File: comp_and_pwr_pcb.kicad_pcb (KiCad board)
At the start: 2 copper layers, 2 parts, among them J2 Conn_01x02, U1 RP2040

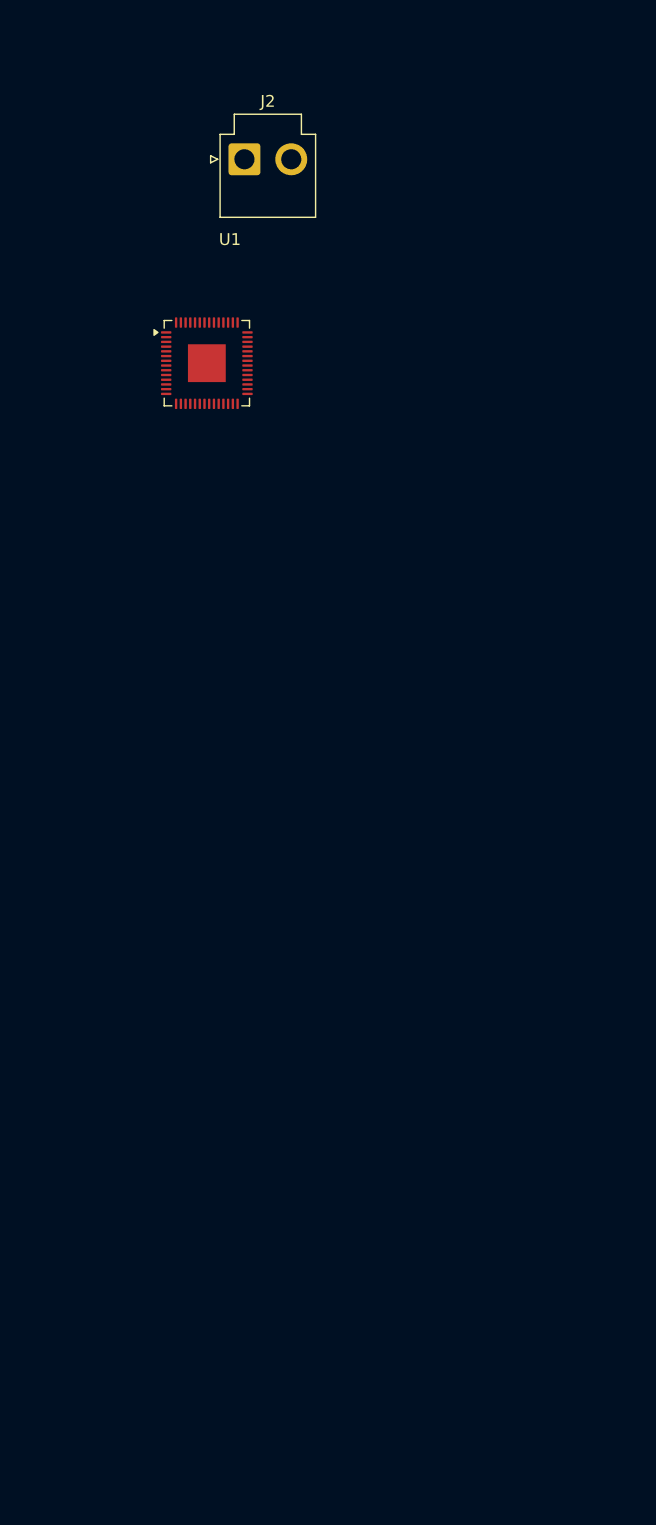
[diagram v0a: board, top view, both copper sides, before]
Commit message: Footprints added and layout finished
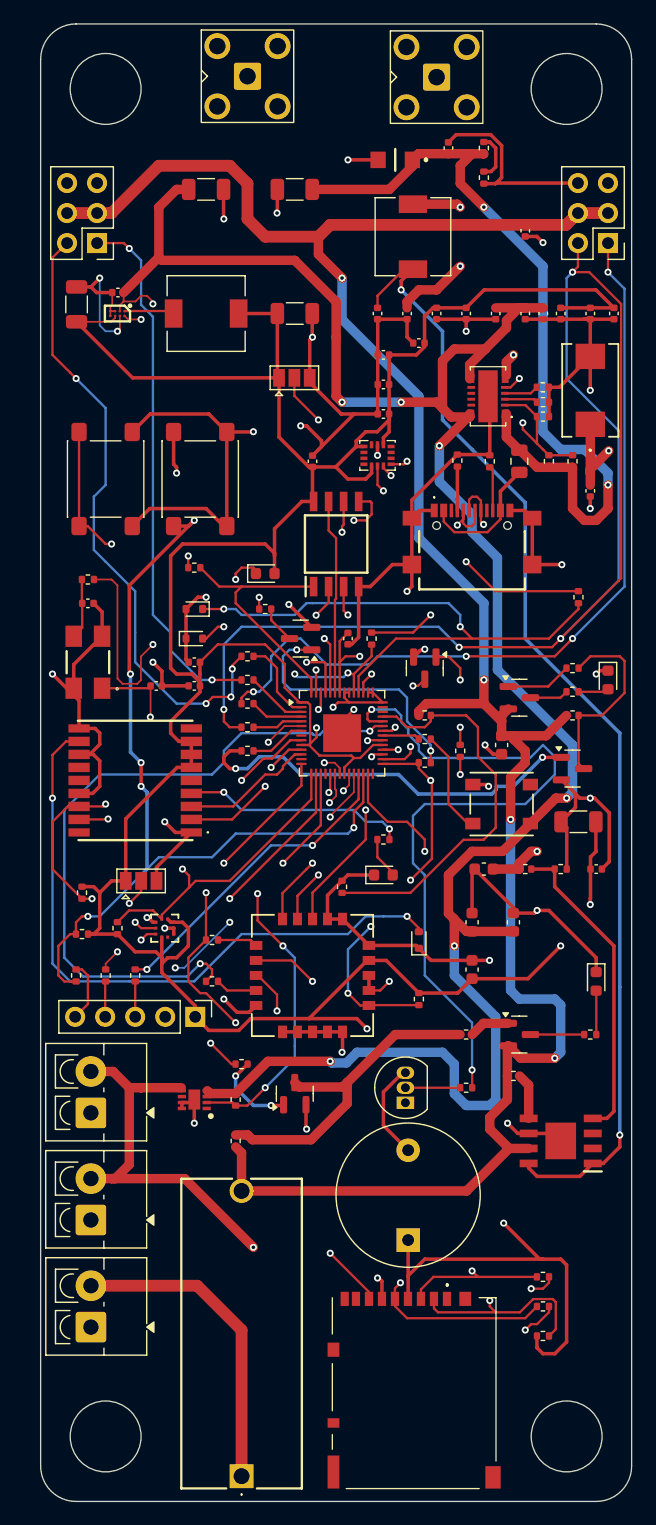
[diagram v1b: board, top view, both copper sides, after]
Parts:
- added 0.1uF: 0.1uF, Capacitor_SMD:C_0402_1005Metric, F.Cu at (136.0, 67.5)
- added 0.1uF: 0.1uF, Capacitor_SMD:C_0402_1005Metric, F.Cu at (129.5, 60.5)
- added 100: 100Ω, Resistor_SMD:R_0402_1005Metric, F.Cu at (137.5, 156.0)
- added 100: 100Ω, Resistor_SMD:R_0402_1005Metric, F.Cu at (137.5, 158.5)
- added 100k: 100k, Resistor_SMD:R_0402_1005Metric, F.Cu at (132.5, 63.0)
- added 100nF: 100nF, Capacitor_SMD:C_0402_1005Metric, F.Cu at (101.5, 72.7)
- added 10k: 10K, Resistor_SMD:R_0402_1005Metric, F.Cu at (137.5, 161.0)
- added 10k: 10k, Resistor_SMD:R_0402_1005Metric, F.Cu at (132.5, 60.5)
- added 10k: 100k, Resistor_SMD:R_0402_1005Metric, F.Cu at (111.5, 144.5)
- added 10uF: 10uF, Capacitor_SMD:C_1206_3216Metric, F.Cu at (98.0, 73.7)
- added 10uF: 10uF, Capacitor_SMD:C_1206_3216Metric, F.Cu at (116.5, 64.0)
- added 10uF: 10uF, Capacitor_SMD:C_1206_3216Metric, F.Cu at (109.0, 64.0)
- added 10uH: 10uH, Inductor_SMD:L_6.3x6.3_H3, F.Cu at (126.5, 68.0)
- added 2.2uH: 2.2uH, Inductor_SMD:L_6.3x6.3_H3, F.Cu at (109.0, 74.5)
- added 3.3V REG: TPS62743YFPR, TPS62743YFPR:BGA8C40P2X4_87X156X53, F.Cu at (101.5, 74.5)
- added 4.7uF: 47 µF, Capacitor_SMD:C_1206_3216Metric, F.Cu at (116.5, 74.5)
- added 5V_REG: TPS5430MDDAREP, TPS5430MDDAREP:SOIC127P600X170-9N, F.Cu at (139.0, 144.5)
- added BUZZER: Buzzer, Buzzer_Beeper:Buzzer_12x9.5RM7.6, F.Cu at (126.1, 152.9)
- added C1: 30pF, Capacitor_SMD:C_0402_1005Metric, F.Cu at (104.8, 106.0)
- added C10: 4.7uF, Capacitor_SMD:C_0402_1005Metric, F.Cu at (137.5, 74.5)
- added C11: 0.1uF, Capacitor_SMD:C_0402_1005Metric, F.Cu at (133.5, 74.5)
- added C12: 4.7uF, Capacitor_SMD:C_0603_1608Metric, F.Cu at (135.0, 126.0)
- added C13: 4.7uF, Capacitor_SMD:C_0603_1608Metric, F.Cu at (131.5, 126.0)
- added C14: 10uF, Capacitor_SMD:C_1206_3216Metric, F.Cu at (140.5, 117.5)
- added C15: 1uF, Capacitor_SMD:C_0402_1005Metric, F.Cu at (124.0, 83.0)
- added C16: 0.1uF, Capacitor_SMD:C_0402_1005Metric, F.Cu at (142.0, 121.5)
- added C17: 0.1uF, Capacitor_SMD:C_0402_1005Metric, F.Cu at (128.5, 74.5)
- added C18: 0.1uF, Capacitor_SMD:C_0402_1005Metric, F.Cu at (127.0, 77.0)
- added C19: 1uF, Capacitor_SMD:C_0402_1005Metric, F.Cu at (121.0, 102.0)
- added C21: 100nF, Capacitor_SMD:C_0402_1005Metric, F.Cu at (124.0, 80.5)
- added C22: 10uF, Capacitor_SMD:C_0402_1005Metric, F.Cu at (143.5, 74.5)
- added C28: 0.1uF, Capacitor_SMD:C_0402_1005Metric, F.Cu at (136.0, 74.5)
- added C29: 0.1uF, Capacitor_SMD:C_0402_1005Metric, F.Cu at (141.5, 89.5)
- added C3: 30pF, Capacitor_SMD:C_0402_1005Metric, F.Cu at (99.0, 99.0)
- added C30: 6TPF470MFH, 6TPF470MFH:6TPF470MFH, F.Cu at (141.5, 81.0)
- added C34: 100nF, Capacitor_SMD:C_0402_1005Metric, F.Cu at (141.5, 74.5)
- added C35: 10µF, Capacitor_SMD:C_0402_1005Metric, F.Cu at (124.0, 78.0)
- added C38: 100nF, Capacitor_SMD:C_0402_1005Metric, F.Cu at (108.0, 104.0)
- added C40: 100nF, Capacitor_SMD:C_0402_1005Metric, F.Cu at (131.0, 74.5)
- added C41: 100nF, Capacitor_SMD:C_0402_1005Metric, F.Cu at (139.0, 74.5)
- added C42: 10uF, Capacitor_SMD:C_0603_1608Metric, F.Cu at (131.5, 130.0)
- added C43: 100nF, Capacitor_SMD:C_0402_1005Metric, F.Cu at (118.0, 87.0)
- added C51: 100nF, Capacitor_SMD:C_0402_1005Metric, F.Cu at (108.0, 106.0)
- added C6: 10uF, Capacitor_SMD:C_0603_1608Metric, F.Cu at (134.0, 111.0)
- added C7: 0.01uF, Capacitor_SMD:C_0402_1005Metric, F.Cu at (123.5, 74.5)
- added C8: 0.1uF, Capacitor_SMD:C_0402_1005Metric, F.Cu at (126.0, 74.5)
- added C9: 10uF, Capacitor_SMD:C_0603_1608Metric, F.Cu at (132.5, 121.5)
- added CAM: CAMERA_CONN_01, TerminalBlock_4Ucon:TerminalBlock_4Ucon_1x02_P3.50mm_Vertical, F.Cu at (99.3, 151.2)
- added CAM: CAMERA_CONN_02, TerminalBlock_4Ucon:TerminalBlock_4Ucon_1x02_P3.50mm_Vertical, F.Cu at (99.3, 142.1)
- added CAM_MOSFET: TPS259531DSGR, TPS259531DSGR:SON50P200X200X80-9N, F.Cu at (108.0, 141.0)
- added D1: ESD5Zxx, Diode_SMD:D_SOD-523, F.Cu at (108.0, 99.5)
- added D2: ESD5Zxx, Diode_SMD:D_SOD-523, F.Cu at (108.0, 102.0)
- added D5: D_TVS, Diode_SMD:D_SOD-523, F.Cu at (127.0, 127.5)
- added E22-400M22S1: ~, E22-400M22S1:E22-400MM22S, F.Cu at (118.0, 130.5)
- added F2: 2016L200PR, Fuse:Fuse_0805_2012Metric, F.Cu at (135.5, 87.0)
- added FLASH_SW: SW_Push, Button_Switch_SMD:SW_SPST_PTS645Sx43SMTR92, F.Cu at (100.5, 88.5)
- added FUSE: 05200101Z, 05200101Z:05200101Z, F.Cu at (112.0, 172.9)
- added GPS: ~, Connector_Coaxial:SMA_BAT_Wireless_BWSMA-KWE-Z001, F.Cu at (128.5, 54.5)
- added IC2: ICM-42688-P, ICM-42688-P:IIM42352, F.Cu at (123.5, 86.5)
- added IC3: LTC4415EDHC#TRPBF, LTC4415EDHC#TRPBF:LTC4415IDHCTRPBF, F.Cu at (131.5, 81.5)
- added IC5: BMP388, BMP388:BMP388, F.Cu at (105.5, 126.5)
- added IC6: W25Q32JVSSIQ, W25Q32JVSSIQ:SOIC127P790X216-8N, F.Cu at (120.0, 94.0)
- added J1: USB4216-03-A, USB4216-03-A:USB421603A, F.Cu at (131.5, 94.5)
- added J3: SWD_CONN, Connector_PinHeader_2.54mm:PinHeader_1x05_P2.54mm_Vertical, F.Cu at (108.1, 134.0)
- added JP1: SolderJumper_3_Open, Jumper:SolderJumper-3_P1.3mm_Open_Pad1.0x1.5mm, F.Cu at (103.5, 122.5)
- added JP4: SolderJumper_3_Open, Jumper:SolderJumper-3_P1.3mm_Open_Pad1.0x1.5mm, F.Cu at (116.5, 79.9)
- added LoRa: ~, Connector_Coaxial:SMA_BAT_Wireless_BWSMA-KWE-Z001, F.Cu at (112.5, 54.4)
- added Q1: 2N3904, Package_TO_SOT_THT:TO-92_Inline, F.Cu at (125.9, 141.3)
- added Q10: PMV28XPEAR, Package_TO_SOT_SMD:SOT-23, F.Cu at (135.5, 135.5)
- added Q4: BC847B, Package_TO_SOT_SMD:SOT-23, F.Cu at (127.5, 104.5)
- added Q5: BC847B, Package_TO_SOT_SMD:SOT-23, F.Cu at (117.0, 102.0)
- added Q7: 2N7002Q-7-F, Package_TO_SOT_SMD:SOT-23, F.Cu at (140.0, 113.0)
- added Q8: PMV28XPEAR, Package_TO_SOT_SMD:SOT-23, F.Cu at (135.5, 107.0)
- added Q9: 2N7002Q-7-F, Package_TO_SOT_SMD:SOT-23, F.Cu at (116.5, 140.5)
- added R1: 1k, Resistor_SMD:R_0402_1005Metric, F.Cu at (99.0, 97.0)
- added R10: 124, Resistor_SMD:R_0402_1005Metric, F.Cu at (137.5, 82.0)
- added R11: 100k, Resistor_SMD:R_0402_1005Metric, F.Cu at (140.0, 87.0)
- added R12: 33, Resistor_SMD:R_0402_1005Metric, F.Cu at (100.5, 130.5)
- added R13: 33, Resistor_SMD:R_0402_1005Metric, F.Cu at (103.0, 130.5)
- added R14: 1k, Resistor_SMD:R_0402_1005Metric, F.Cu at (98.0, 130.5)
- added R15: 10k, Resistor_SMD:R_0402_1005Metric, F.Cu at (98.5, 127.0)
- added R16: 10k, Resistor_SMD:R_0402_1005Metric, F.Cu at (127.5, 108.5)
- added R17: 5.6k, Resistor_SMD:R_0402_1005Metric, F.Cu at (120.5, 123.0)
- added R18: 100, Resistor_SMD:R_0402_1005Metric, F.Cu at (112.5, 105.5)
- added R19: 100, Resistor_SMD:R_0402_1005Metric, F.Cu at (112.5, 103.5)
- added R2: 5.1k, Resistor_SMD:R_0402_1005Metric, F.Cu at (130.3, 86.9)
- added R20: 1kΩ, Resistor_SMD:R_0402_1005Metric, F.Cu at (131.0, 140.0)
- added R21: 21.5k, Resistor_SMD:R_0402_1005Metric, F.Cu at (137.5, 83.2)
- added R22: 100, Resistor_SMD:R_0402_1005Metric, F.Cu at (112.5, 107.5)
- added R23: 100, Resistor_SMD:R_0402_1005Metric, F.Cu at (112.5, 109.5)
- added R28: 100k, Resistor_SMD:R_0402_1005Metric, F.Cu at (111.5, 141.0)
- added R3: 5.1k, Resistor_SMD:R_0402_1005Metric, F.Cu at (133.0, 87.0)
- added R32: 15.8k, Resistor_SMD:R_0402_1005Metric, F.Cu at (127.5, 110.5)
- added R35: 100Ω, Resistor_SMD:R_0402_1005Metric, F.Cu at (109.5, 127.5)
- added R38: 100Ω, Resistor_SMD:R_0402_1005Metric, F.Cu at (109.5, 131.0)
- added R39: 10kΩ, Resistor_SMD:R_0402_1005Metric, F.Cu at (127.0, 132.5)
- added R4: 22, Resistor_SMD:R_0402_1005Metric, F.Cu at (140.5, 98.5)
- added R40: 10kΩ, Resistor_SMD:R_0402_1005Metric, F.Cu at (130.5, 111.5)
- added R41: 220Ω, Resistor_SMD:R_0402_1005Metric, F.Cu at (127.5, 112.5)
- added R42: 220Ω, Resistor_SMD:R_0402_1005Metric, F.Cu at (114.0, 99.5)
- added R43: 4.7K, Resistor_SMD:R_0402_1005Metric, F.Cu at (101.5, 126.5)
- added R44: 4.7K, Resistor_SMD:R_0402_1005Metric, F.Cu at (98.5, 123.5)
- added R48: 220Ω, Resistor_SMD:R_0402_1005Metric, F.Cu at (124.0, 119.0)
- added R5: 22, Resistor_SMD:R_0402_1005Metric, F.Cu at (123.0, 102.0)
- added R54: 1kΩ, Resistor_SMD:R_0402_1005Metric, F.Cu at (108.0, 96.0)
- added R57: 100k, Resistor_SMD:R_0402_1005Metric, F.Cu at (140.0, 108.5)
- added R58: 47, Resistor_SMD:R_0402_1005Metric, F.Cu at (140.0, 104.5)
- added R59: 10k, Resistor_SMD:R_0402_1005Metric, F.Cu at (112.5, 111.5)
- added R6: 100k, Resistor_SMD:R_0402_1005Metric, F.Cu at (135.0, 139.0)
- added R60: 3.3k, Resistor_SMD:R_0402_1005Metric, F.Cu at (140.0, 106.5)
- added R61: 10k, Resistor_SMD:R_0402_1005Metric, F.Cu at (112.0, 138.0)
- added R62: 47, Resistor_SMD:R_0402_1005Metric, F.Cu at (131.0, 135.5)
- added R64: 3.3k, Resistor_SMD:R_0402_1005Metric, F.Cu at (141.5, 135.5)
- added R7: 10k, Resistor_SMD:R_0402_1005Metric, F.Cu at (136.0, 121.5)
- added R8: 3.24k, Resistor_SMD:R_0402_1005Metric, F.Cu at (139.0, 121.5)
- added R9: 47k, Resistor_SMD:R_0402_1005Metric, F.Cu at (138.0, 87.0)
- added R9: 124, Resistor_SMD:R_0402_1005Metric, F.Cu at (137.5, 80.7)
- added SD_CARD: DM3AT-SF-PEJM5, DM3AT-SF-PEJM5:DM3ATSFPEJM5, F.Cu at (126.6, 165.3)
- added SERVO: SERVO_CONN_02, Connector_PinHeader_2.54mm:PinHeader_2x03_P2.54mm_Vertical, F.Cu at (143.0, 68.5)
- added SERVO: SERVO_CONN_01, Connector_PinHeader_2.54mm:PinHeader_2x03_P2.54mm_Vertical, F.Cu at (99.8, 68.5)
- added STATUS1: WS2812B, WS2812B:WS2812B, F.Cu at (134.0, 116.0)
- added SWD_SW: SW_Push, Button_Switch_SMD:SW_SPST_PTS645Sx43SMTR92, F.Cu at (108.5, 88.5)
- added SZSMF6L5.0AT3G: SZSMF6L5.0AT3G, SZSMF6L5.0AT3G:SMFA2005CA, F.Cu at (125.0, 61.5)
- added TX1: XL-1608UBC-04, LED_SMD:LED_0603_1608Metric, F.Cu at (114.0, 96.5)
- added TX2: XL-1608UBC-04, LED_SMD:LED_0603_1608Metric, F.Cu at (143.0, 105.5)
- added TX3: XL-1608UBC-04, LED_SMD:LED_0603_1608Metric, F.Cu at (142.0, 131.0)
- added TX4: XL-1608UBC-04, LED_SMD:LED_0603_1608Metric, F.Cu at (124.0, 122.0)
- added U2: MAX-M10S, MAX-M10S:MAXM10M00B, F.Cu at (103.0, 114.0)
- added Y1: ABMM2-12.000MHZ-D1-T, ABMM2-12.000MHZ-D1-T:ABMM2, F.Cu at (99.0, 104.0)
- BATT: renamed from J2; value Conn_01x02 -> BATTERY_CONN; footprint Connector_JST:JST_VH_B2P-VH-B_1x02_P3.96mm_Vertical -> TerminalBlock_4Ucon:TerminalBlock_4Ucon_1x02_P3.50mm_Vertical
- moved BATT 99.6 mm to (99.3, 160.2), turned to 90 degrees
- moved U1 33.3 mm to (120.5, 110.0)
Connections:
- BATT pad 1: unconnected-(J2-Pin_1-Pad1) -> GND
- BATT pad 2: unconnected-(J2-Pin_2-Pad2) -> Net-(J2-Pin_2)
- U1 pad 1: Net-(U1-IOVDD-Pad1) -> +3.3V
- U1 pad 10: Net-(U1-IOVDD-Pad1) -> +3.3V
- U1 pad 11: unconnected-(U1-GPIO8-Pad11) -> /UART_TX
- U1 pad 12: unconnected-(U1-GPIO9-Pad12) -> /UART_RX
- U1 pad 14: unconnected-(U1-GPIO11-Pad14) -> /SPI_MISO
- U1 pad 15: unconnected-(U1-GPIO12-Pad15) -> /I2C_SCL
- U1 pad 16: unconnected-(U1-GPIO13-Pad16) -> /I2C_SDA
- U1 pad 17: unconnected-(U1-GPIO14-Pad17) -> /SPI_MOSI
- U1 pad 19: unconnected-(U1-TESTEN-Pad19) -> GND
- U1 pad 2: unconnected-(U1-GPIO0-Pad2) -> /SERVO_1
- U1 pad 20: Net-(U1-XIN) -> /X_IN
- U1 pad 21: Net-(U1-XOUT) -> /X_OUT
- U1 pad 22: Net-(U1-IOVDD-Pad1) -> +3.3V
- U1 pad 23: Net-(U1-DVDD-Pad23) -> Net-(U1-VREG_VOUT)
- U1 pad 24: unconnected-(U1-SWCLK-Pad24) -> /SWCLK
- U1 pad 25: unconnected-(U1-SWD-Pad25) -> /SWDIO
- U1 pad 26: unconnected-(U1-RUN-Pad26) -> /RUN
- U1 pad 27: unconnected-(U1-GPIO16-Pad27) -> /SPI_SCK
- U1 pad 29: unconnected-(U1-GPIO18-Pad29) -> /TXEN
- U1 pad 3: unconnected-(U1-GPIO1-Pad3) -> /SERVO_2
- U1 pad 30: unconnected-(U1-GPIO19-Pad30) -> /RXEN
- U1 pad 31: unconnected-(U1-GPIO20-Pad31) -> /DIO1
- U1 pad 32: unconnected-(U1-GPIO21-Pad32) -> /IO0
- U1 pad 33: Net-(U1-IOVDD-Pad1) -> +3.3V
- U1 pad 34: unconnected-(U1-GPIO22-Pad34) -> /IO1
- U1 pad 35: unconnected-(U1-GPIO23-Pad35) -> /STAT_LED
- U1 pad 36: unconnected-(U1-GPIO24-Pad36) -> /CS_MICROSD
- U1 pad 37: unconnected-(U1-GPIO25-Pad37) -> /NSS
- U1 pad 38: unconnected-(U1-GPIO26_ADC0-Pad38) -> /BUZZER
- U1 pad 39: unconnected-(U1-GPIO27_ADC1-Pad39) -> /V_BATT_READOUT
- U1 pad 4: unconnected-(U1-GPIO2-Pad4) -> /SERVO_3
- U1 pad 42: Net-(U1-IOVDD-Pad1) -> +3.3V
- U1 pad 43: unconnected-(U1-ADC_AVDD-Pad43) -> +3.3V
- U1 pad 44: unconnected-(U1-VREG_IN-Pad44) -> +3.3V
- U1 pad 45: unconnected-(U1-VREG_VOUT-Pad45) -> Net-(U1-VREG_VOUT)
- U1 pad 46: unconnected-(U1-USB_DM-Pad46) -> /USB_DM
- U1 pad 47: unconnected-(U1-USB_DP-Pad47) -> /USB_DP
- U1 pad 48: unconnected-(U1-USB_VDD-Pad48) -> +3.3V
- U1 pad 49: Net-(U1-IOVDD-Pad1) -> +3.3V
- U1 pad 5: unconnected-(U1-GPIO3-Pad5) -> /SERVO_4
- U1 pad 50: Net-(U1-DVDD-Pad23) -> Net-(U1-VREG_VOUT)
- U1 pad 51: unconnected-(U1-QSPI_SD3-Pad51) -> /QSPI_SD3
- U1 pad 52: unconnected-(U1-QSPI_SCLK-Pad52) -> /QSPI_SCLK
- U1 pad 53: unconnected-(U1-QSPI_SD0-Pad53) -> /QSPI_SD0
- U1 pad 54: unconnected-(U1-QSPI_SD2-Pad54) -> /QSPI_SD2
- U1 pad 55: unconnected-(U1-QSPI_SD1-Pad55) -> /QSPI_SD1
- U1 pad 56: unconnected-(U1-QSPI_SS-Pad56) -> /WSP_SS
- U1 pad 57: unconnected-(U1-GND-Pad57) -> GND
- U1 pad 6: unconnected-(U1-GPIO4-Pad6) -> /CAMERA_SWITCH
- U1 pad 7: unconnected-(U1-GPIO5-Pad7) -> /PYRO1_SW
- U1 pad 9: unconnected-(U1-GPIO7-Pad9) -> /PYRO2_SW
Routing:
- net +3.3V: track 0.00 -> 323.5 mm, vias 0 -> 6
- net GND: track 0.00 -> 314.2 mm, vias 0 -> 37
- net +BATT: track 0.00 -> 190.8 mm, vias 0 -> 4
- net +5V: track 0.00 -> 183.9 mm, vias 0 -> 8
- net Net-(C30-+): track 0.00 -> 153.9 mm, vias 0 -> 2
- net Net-(J5-Pin_2): track 0.00 -> 111.7 mm, vias 0 -> 4
- net /SPI_SCK: track 0.00 -> 97.1 mm, vias 0 -> 2
- net Net-(IC1-BOOT): track 0.00 -> 96.7 mm, vias 0 -> 2
- net /I2C_SDA: track 0.00 -> 95.2 mm, vias 0 -> 5
- net /CS_MICROSD: track 0.00 -> 88.7 mm, vias 0 -> 2
- net /5V_BATT: track 0.00 -> 84.9 mm, vias 0 -> 4
- net /I2C_SCL: track 0.00 -> 82.0 mm, vias 0 -> 3
- net /RUN: track 0.00 -> 81.8 mm, vias 0 -> 7
- net /SPI_MOSI: track 0.00 -> 75.4 mm, vias 0 -> 2
- net Net-(J5-Pin_1): track 0.00 -> 69.4 mm, vias 0 -> 4
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- added copper zone on In1.Cu, net GND
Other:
- board outline added: 50 x 125 mm
- copper layers 2 -> 4

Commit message: Replaced files and updated project
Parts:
- removed 100k: 100k, Resistor_SMD:R_0402_1005Metric
- removed 10k: 10k, Resistor_SMD:R_0402_1005Metric
- removed 10uF: 10uF, Capacitor_SMD:C_1206_3216Metric
- removed FUSE: 05200101Z, 05200101Z:05200101Z
- removed GPS, LoRa: ~, Connector_Coaxial:SMA_BAT_Wireless_BWSMA-KWE-Z001
- added D5: D_TVS, Diode_SMD:D_SOD-523, F.Cu at (140.0, 104.8)
- added F1: Fuse_Small, Fuse:Fuse_0402_1005Metric, F.Cu at (114.1, 171.5)
- added J10: Conn_01x02, TerminalBlock_4Ucon:TerminalBlock_4Ucon_1x02_P3.50mm_Vertical, F.Cu at (99.4, 122.9)
- added J11: Conn_Coaxial, Connector_Coaxial:SMA_Molex_73251-2200_Horizontal, F.Cu at (111.5, 91.0)
- added J12: Conn_Coaxial, Connector_Coaxial:SMA_Molex_73251-2200_Horizontal, F.Cu at (127.5, 91.0)
- added J9: Conn_01x02, TerminalBlock_4Ucon:TerminalBlock_4Ucon_1x02_P3.50mm_Vertical, F.Cu at (99.4, 132.0)
- added R24: 4.7kΩ, Resistor_SMD:R_0402_1005Metric, F.Cu at (140.8, 147.3)
- C2, C39: renamed from 10uF; moved to B.Cu
- C4: renamed from 0.1uF; moved to B.Cu
- C40, D1, D2, F2, J1, R2, R3, R4, R5: moved to B.Cu
- D4: renamed from SZSMF6L5.0AT3G; moved to B.Cu
- E22-400M22S1: footprint E22-400M22S1:E22-400MM22S -> E22-400M22S:E22-400M22S; moved to B.Cu
- IC7: renamed from 3.3V REG
- J6: renamed from SD_CARD; moved to B.Cu
- moved C4 107.6 mm to (106.7, 165.6), turned to -90 degrees
- moved C5 106.6 mm to (112.9, 171.5), turned to 90 degrees
- moved D4 105.0 mm to (112.0, 165.7), turned to -90 degrees
- moved C2 102.0 mm to (108.7, 165.7), turned to -90 degrees
- moved C7 98.9 mm to (125.6, 173.4), turned to 90 degrees
- moved C28 96.3 mm to (111.0, 167.5)
- moved L1 96.1 mm to (121.1, 163.9)
- moved C8 87.9 mm to (115.1, 161.7)
- moved C30 87.1 mm to (109.5, 162.0), turned to 0 degrees
- moved C29 83.6 mm to (106.5, 165.5), turned to 0 degrees
- moved R9 82.0 mm to (110.4, 158.2), turned to 90 degrees
- moved R10 81.3 mm to (109.1, 158.2), turned to 90 degrees
- moved R21 80.7 mm to (107.8, 158.2), turned to 90 degrees
- moved C10 80.3 mm to (110.3, 150.0), turned to 180 degrees
- moved F2 79.4 mm to (116.8, 164.2), turned to 180 degrees
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- renumbered BUZZER to BZ1, 4.7uF to C36, 0.1uF to C5, 100nF to C52, 5V_REG to IC1, CAM_MOSFET to IC4, BATT to J2, SERVO to J4, SERVO to J5, CAM to J7, CAM to J8, 10uH to L1, 2.2uH to L2, 100 to R36, 100 to R37, 10k to R45, 10k to R63, SWD_SW to SW1, FLASH_SW to SW2
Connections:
- D5 pad 2: Net-(D5-A2) -> /RF_IN
- Q7 pad 2: GND -> Net-(J10-Pin_1)
- Q9 pad 2: GND -> Net-(J9-Pin_1)
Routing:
- net +5V: track 183.9 -> 53.1 mm, vias 8 -> 2
- net Net-(C30-+): track 153.9 -> 34.8 mm, vias 2 -> 0
- net Net-(J5-Pin_2): track 111.7 -> 23.4 mm, vias 4 -> 2
- net +3.3V: track 323.5 -> 244.4 mm, vias 6 -> 9
- net Net-(IC1-BOOT): track 96.7 -> 20.0 mm, vias 2 -> 0
- net /5V_BATT: track 84.9 -> 18.9 mm, vias 4 -> 0
- net /CS_MICROSD: track 88.7 -> 34.5 mm, vias 2 -> 3
- net Net-(E22-400M22S1-SCK): track 46.7 -> 2.58 mm, vias 2 -> 1
- net /SPI_SCK: track 97.1 -> 53.3 mm
- net Net-(J5-Pin_1): track 69.4 -> 26.6 mm, vias 4 -> 0
- net Net-(E22-400M22S1-MOSI): track 43.1 -> 2.58 mm, vias 2 -> 1
- net /RUN: track 81.8 -> 43.1 mm, vias 7 -> 2
- net /5V_USB: track 68.9 -> 30.5 mm, vias 2 -> 1
- net /USB_DP: track 19.9 -> 57.1 mm
- net GND: track 314.2 -> 277.6 mm, vias 37 -> 40
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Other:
- board size 50 x 125 mm -> 50 x 88.5 mm

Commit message: Initial KiCad project commit
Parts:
- removed C14: 10uF, Capacitor_SMD:C_1206_3216Metric
- removed the D5 at (139.4, 102.4)
- removed IC7: TPS62743YFPR, TPS62743YFPR:BGA8C40P2X4_87X156X53
- added C20: 0.1uF, Capacitor_SMD:C_0402_1005Metric, B.Cu at (104.5, 144.5)
- added C23: 4.7uF, Capacitor_SMD:C_0603_1608Metric, B.Cu at (108.6, 147.2)
- added C24: 10uF, Capacitor_SMD:C_1206_3216Metric, B.Cu at (110.8, 150.1)
- added H1: MountingHole, MountingHole:MountingHole_3.2mm_M3, F.Cu at (101.0, 169.0)
- added H2: MountingHole, MountingHole:MountingHole_3.2mm_M3, F.Cu at (139.0, 169.0)
- added H3: MountingHole, MountingHole:MountingHole_3.2mm_M3, F.Cu at (139.0, 92.5)
- added H4: MountingHole, MountingHole:MountingHole_3.2mm_M3, F.Cu at (101.0, 92.5)
- added R25: 100k, Resistor_SMD:R_0402_1005Metric, B.Cu at (106.8, 146.2)
- added R26: 6.8k, Resistor_SMD:R_0402_1005Metric, B.Cu at (108.6, 149.7)
- added R27: 26.1k, Resistor_SMD:R_0402_1005Metric, B.Cu at (110.1, 146.6)
- added R29: 10k, Resistor_SMD:R_0402_1005Metric, B.Cu at (111.2, 146.6)
- added U3: MP2307DN-LF-Z, MP2307DN-LF-Z:SOIC127P600X170-9N, B.Cu at (108.0, 141.5)
- BZ1: footprint Buzzer_Beeper:Buzzer_12x9.5RM7.6 -> Buzzer_Beeper:Buzzer_CUI_CPT-9019S-SMT
- C11: value 0.1uF -> 10uF; footprint Capacitor_SMD:C_0402_1005Metric -> Capacitor_SMD:C_1206_3216Metric; moved to B.Cu
- C12: value 4.7uF -> 0.1nF; footprint Capacitor_SMD:C_0603_1608Metric -> Capacitor_SMD:C_0402_1005Metric; moved to B.Cu
- C13: value 4.7uF -> 10uF; footprint Capacitor_SMD:C_0603_1608Metric -> Capacitor_SMD:C_1206_3216Metric; moved to B.Cu
- L2: value 2.2uH -> 10uH; moved to B.Cu
- moved J1 53.4 mm to (142.0, 121.5), turned to -90 degrees
- moved D1 47.3 mm to (133.5, 117.7), turned to 0 degrees
- moved R2 46.1 mm to (133.5, 119.4), turned to 180 degrees
- moved R4 45.3 mm to (133.5, 120.5), turned to 0 degrees
- moved R5 44.5 mm to (133.5, 121.7), turned to 0 degrees
- moved R3 43.8 mm to (133.5, 122.8), turned to 180 degrees
- moved F2 42.2 mm to (134.1, 125.8), turned to -90 degrees
- moved C4 42.1 mm to (135.3, 134.7), turned to 0 degrees
- moved D4 42.1 mm to (133.5, 129.5), turned to 0 degrees
- moved C2 41.1 mm to (133.5, 133.0), turned to 0 degrees
- moved D2 39.1 mm to (132.1, 125.0), turned to 90 degrees
- moved C12 12.3 mm to (107.4, 136.6), turned to 0 degrees
- moved C13 11.1 mm to (107.0, 152.0), turned to 180 degrees
- moved C11 7.15 mm to (105.4, 148.1)
- moved L2 5.48 mm to (114.5, 141.5), turned to -90 degrees
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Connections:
- C12 pad 1: +5V -> /3.3V_BS
- C12 pad 2: GND -> Net-(U3-SW)
- C13 pad 1: +5V -> Net-(C13-Pad1)
- L2 pad 1: Net-(IC7-SW) -> Net-(U3-SW)
- Q10 pad 3: Net-(Q10-D) -> Net-(J9-Pin_1)
- Q7 pad 2: Net-(J10-Pin_1) -> GND
- Q8 pad 3: Net-(Q8-D) -> Net-(J10-Pin_1)
- Q9 pad 2: Net-(J9-Pin_1) -> GND
- R60 pad 1: Net-(Q8-D) -> Net-(J10-Pin_1)
- R64 pad 1: Net-(Q10-D) -> Net-(J9-Pin_1)
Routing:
- net /5V_USB: track 30.5 -> 80.3 mm, vias 1 -> 4
- net Net-(J10-Pin_1): track 17.0 -> 55.7 mm, vias 0 -> 1
- net +5V: track 53.1 -> 77.0 mm, vias 2 -> 8
- net +BATT: track 156.4 -> 179.1 mm, vias 4 -> 5
- net Net-(J9-Pin_1): track 12.9 -> 25.2 mm, vias 0 -> 1
- net /USB_DP: track 57.1 -> 45.3 mm
- net /QSPI_SD1: track 14.3 -> 25.7 mm
- net Net-(U3-SW): track 0.00 -> 10.7 mm
- net GND: track 277.6 -> 269.1 mm
- net /I2C_SCL: track 90.7 -> 99.0 mm, vias 5 -> 6
- net Net-(IC7-SW): track 5.25 -> 0.00 mm, vias 2 -> 0
- net +3.3V: track 244.4 -> 240.8 mm, vias 9 -> 8
- net /SWDIO: track 41.6 -> 44.8 mm
- net Net-(J1-DP1): track 4.70 -> 7.56 mm
- net Net-(J2-Pin_2): track 25.8 -> 23.0 mm, vias 0 -> 2
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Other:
- outline, holes or cut-outs redrawn

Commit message: Just a commit
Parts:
- added C14: 10uF, Capacitor_SMD:C_0402_1005Metric, F.Cu at (139.0, 152.5)
- added C25: 100nF, Capacitor_SMD:C_0402_1005Metric, F.Cu at (139.0, 153.5)
- added R24: 5k, Resistor_SMD:R_0402_1005Metric, F.Cu at (106.5, 169.5)
- added R30: 10K, Resistor_SMD:R_0402_1005Metric, F.Cu at (110.0, 127.0)
- IC3: footprint LTC4415EDHC#TRPBF:LTC4415IDHCTRPBF -> Package_DFN_QFN:DFN-18-1EP_3x5mm_P0.5mm_EP1.66x4.4mm
- Q1: footprint Package_TO_SOT_THT:TO-92_Inline -> Package_TO_SOT_SMD:SOT-23
- moved C1 5.16 mm to (110.5, 125.0), turned to 180 degrees
- moved R16 1.05 mm to (111.5, 173.5)
- moved R17 1.05 mm to (110.7, 171.6)
- moved C5 1.05 mm to (113.9, 171.6)
- moved C6 1.05 mm to (112.3, 171.5)
- moved F1 1.05 mm to (115.2, 171.5)
- moved IC3 0.92 mm to (109.2, 153.4)
- moved C10 0.49 mm to (110.3, 149.5)
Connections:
- C24 pad 1: Net-(C24-Pad1) -> +3.3V
- C7 pad 2: GND -> Net-(IC1-PH)
- D1 pad 1: /USB_DM -> Net-(D1-K)
- D2 pad 2: /USB_DP -> Net-(D2-A)
- IC1 pad 8: Net-(IC1-BOOT) -> Net-(IC1-PH)
- IC3 pad 19: +5V -> /5V_BATT
- IC4 pad 7: GND -> Net-(IC4-ILM)
- J1 pad A6: Net-(J1-DP1) -> Net-(D2-A)
- J1 pad A7: Net-(J1-DN1) -> Net-(D1-K)
- J1 pad B6: Net-(J1-DP1) -> Net-(D2-A)
- J1 pad B7: Net-(J1-DN1) -> Net-(D1-K)
- L1 pad 1: Net-(IC1-BOOT) -> Net-(IC1-PH)
- Q7 pad 1: Net-(Q7-G) -> /PYRO1_SW
- Q9 pad 1: Net-(Q9-G) -> /PYRO2_SW
- R27 pad 1: +3.3V -> Net-(U3-FB)
- R27 pad 2: Net-(C24-Pad1) -> +3.3V
- R29 pad 2: +3.3V -> Net-(U3-FB)
- R4 pad 2: Net-(J1-DN1) -> Net-(D1-K)
- R5 pad 2: Net-(J1-DP1) -> Net-(D2-A)
- R59 pad 2: Net-(Q7-G) -> GND
- R61 pad 2: Net-(Q9-G) -> GND
- U3 pad 5: +3.3V -> Net-(U3-FB)
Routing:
- net /WSP_SS: track 19.3 -> 53.0 mm, vias 2 -> 4
- net Net-(D2-A): track 0.00 -> 19.7 mm, vias 0 -> 2
- net Net-(IC1-BOOT): track 19.4 -> 2.05 mm
- net Net-(D1-K): track 0.00 -> 14.7 mm, vias 0 -> 2
- net Net-(IC1-PH): track 0.00 -> 13.9 mm
- net /5V_USB: track 80.3 -> 90.3 mm
- net Net-(Q1-B): track 4.89 -> 13.4 mm
- net Net-(J1-DP1): track 7.56 -> 0.00 mm
- net Net-(IC3-EN1): track 11.3 -> 18.9 mm
- net Net-(J1-DN1): track 7.44 -> 0.00 mm
- net Net-(E22-400M22S1-ANT): track 32.1 -> 24.7 mm, vias 1 -> 0
- net Net-(IC3-CLIM2): track 2.74 -> 9.37 mm, vias 0 -> 2
- net Net-(IC3-CLIM1): track 2.44 -> 8.94 mm, vias 0 -> 2
- net /5V_BATT: track 18.7 -> 24.2 mm
- net Net-(U3-FB): track 0.00 -> 3.30 mm
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- added copper zone on B.Cu, net GND
- added copper zone on F.Cu, net GND

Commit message: Final commit?
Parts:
- removed Q7, Q9: 2N7002Q-7-F, Package_TO_SOT_SMD:SOT-23
- added Q2: BSS138, Package_TO_SOT_SMD:SOT-23, F.Cu at (110.0, 136.0)
- added Q3: BSS138, Package_TO_SOT_SMD:SOT-23, F.Cu at (109.5, 131.5)
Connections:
- U1 pad 29: /TXEN -> unconnected-(U1-GPIO18-Pad29)
- U1 pad 30: /RXEN -> unconnected-(U1-GPIO19-Pad30)
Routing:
- net /RXEN: track 36.4 -> 6.38 mm, vias 3 -> 1
- net /TXEN: track 43.9 -> 20.3 mm, vias 4 -> 2
- net Net-(IC1-PH): track 13.9 -> 21.2 mm
- net GND: track 270.8 -> 276.9 mm, vias 42 -> 61
- net /PYRO1_SW: track 28.0 -> 25.2 mm
- net /PYRO2_SW: track 41.5 -> 39.1 mm
- net +5V: track 75.4 -> 77.2 mm, vias 7 -> 6
- net Net-(U3-SW): track 10.7 -> 9.98 mm
- net Net-(Q2-D): track 4.47 -> 3.97 mm
